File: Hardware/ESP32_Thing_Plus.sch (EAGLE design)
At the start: 40 parts, among them J1 AMP FCI 10103594-0001LF, Q1 2.5A/30V, Q2 MBT3904DW1T1, U1 MCP73831, U2 ESP-WROOM-32NARROW, U3 AP2112K-3.3V, U4 CP2102N

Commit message: v03 Changes
-Updated size to 2.3x0.9in
- Moved Qwiic connector to top
- Adjusted inner layer copper pour
- Cleaned up traces
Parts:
- added S2: 0, SparkFun-Switches:MOMENTARY-SWITCH-SPST-2-SMD-4.6X2.8MM
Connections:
- net 0: now also S2.4
- net GND: now also S2.1
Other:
- note added: "GPIO0 Button"
- note added: "Revised by: Alex Wende"
- note added: "v03"
- note removed: "02"
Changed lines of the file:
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@@
 <?xml version="1.0" encoding="utf-8"?>
 <!DOCTYPE eagle SYSTEM "eagle.dtd">
-<eagle version="9.0.1">
+<eagle version="9.1.1">
 <drawing>
 <settings>
@@
 <part name="FD3" library="SparkFun-Aesthetics" deviceset="FIDUCIAL" device="UFIDUCIAL"/>
 <part name="FD4" library="SparkFun-Aesthetics" deviceset="FIDUCIAL" device="UFIDUCIAL"/>
+<part name="S2" library="SparkFun-Switches" deviceset="MOMENTARY-SWITCH-SPST-2" device="-SMD-4.6X2.8MM" value="0"/>
+<part name="GND10" library="SparkFun-Aesthetics" deviceset="GND" device=""/>
 </parts>
 <sheets>
@@
 If U0TXD, GPIO2, GPIO5 are floating,
 GPIO0 determines boot mode</text>
-<text x="256.54" y="276.86" size="2.54" layer="94" font="vector" align="top-left">CP2102N (USB-to-Serial Converter)</text>
+<text x="256.54" y="274.32" size="2.54" layer="94" font="vector">CP2102N (USB-to-Serial Converter)</text>
 <text x="134.62" y="264.16" size="1.524" layer="97" align="top-left">V_BATT should be a single-
 cell LiPo battery.</text>
@@
 I_CHG = 1000 / R_PROG
 R_PROG=2k : I_CHG=500mA</text>
-<text x="2.54" y="276.86" size="2.54" layer="94" font="vector" align="top-left">Voltage Regulator and Battery Charger</text>
-<text x="132.08" y="276.86" size="2.54" layer="94" font="vector" align="top-left">Lithium-Polymer Battery Charger (1-cell)</text>
+<text x="2.54" y="274.32" size="2.54" layer="94" font="vector">Voltage Regulator and Battery Charger</text>
+<text x="132.08" y="274.32" size="2.54" layer="94" font="vector">Lithium-Polymer Battery Charger (1-cell)</text>
 <text x="86.36" y="220.98" size="1.778" layer="97" font="vector" align="top-center">600mA out
 6V max in</text>
-<text x="332.74" y="190.5" size="2.54" layer="94" font="vector" align="top-left">Auto-Reset</text>
+<text x="332.74" y="187.96" size="2.54" layer="94" font="vector">Auto-Reset</text>
 <wire x1="0" y1="193.04" x2="129.54" y2="193.04" width="0.2032" layer="97" style="longdash"/>
 <wire x1="129.54" y1="193.04" x2="254" y2="193.04" width="0.2032" layer="97" style="longdash"/>
@@
 <wire x1="259.08" y1="55.88" x2="259.08" y2="0" width="0.2032" layer="97" style="longdash"/>
 <wire x1="259.08" y1="55.88" x2="198.12" y2="55.88" width="0.2032" layer="97" style="longdash"/>
-<text x="2.54" y="190.5" size="2.54" layer="94" align="top-left">Espressif ESP32</text>
-<text x="261.62" y="63.5" size="2.54" layer="94" font="vector" align="top-left">Reset Button</text>
-<text x="332.74" y="104.14" size="2.54" layer="94" font="vector" align="top-left">Headers</text>
-<text x="421.64" y="10.16" size="2.54" layer="94" align="top-left">02</text>
+<text x="2.54" y="187.96" size="2.54" layer="94">Espressif ESP32</text>
+<text x="261.62" y="60.96" size="2.54" layer="94" font="vector">Reset Button</text>
+<text x="332.74" y="101.6" size="2.54" layer="94" font="vector">Headers</text>
+<text x="421.64" y="10.16" size="2.54" layer="94" align="top-left">v03</text>
 <text x="273.812" y="0.762" size="1.778" layer="94" rot="MR180" align="top-left">Original ESP32 Thing by Jim Lindblom</text>
 <text x="381" y="114.3" size="1.778" layer="97" font="vector" align="top-center">If DTR is LOW, toggling RTS from HIGH to LOW resets to run mode.
 If RTS is HIGH, toggling DTR from LOW to HIGH resets to bootloader.</text>
-<text x="264.16" y="187.96" size="2.54" layer="94" font="vector">QWIIC Connector</text>
+<text x="261.62" y="187.96" size="2.54" layer="94" font="vector">QWIIC Connector</text>
 <wire x1="259.08" y1="99.06" x2="259.08" y2="193.04" width="0.1524" layer="97" style="longdash"/>
-<text x="358.14" y="7.62" size="3.81" layer="94">Mike Hord</text>
+<text x="348.996" y="11.43" size="2.54" layer="94">Mike Hord</text>
 <text x="200.66" y="50.8" size="2.54" layer="94" font="vector">GPIO13 LED</text>
+<wire x1="259.08" y1="99.06" x2="259.08" y2="66.04" width="0.1524" layer="97" style="longdash"/>
+<text x="261.62" y="93.98" size="2.54" layer="94">GPIO0 Button</text>
+<text x="331.47" y="6.604" size="2.54" layer="94">Revised by: Alex Wende</text>
 </plain>
 <instances>
@@
 <instance part="FD3" gate="G$1" x="426.72" y="30.48"/>
 <instance part="FD4" gate="G$1" x="429.26" y="30.48"/>
+<instance part="S2" gate="G$1" x="294.64" y="83.82"/>
+<instance part="GND10" gate="1" x="287.02" y="78.74"/>
 </instances>
 <busses>
@@
 <pinref part="GND8" gate="1" pin="GND"/>
 <wire x1="185.42" y1="121.92" x2="185.42" y2="119.38" width="0.1524" layer="91"/>
+</segment>
+<segment>
+<pinref part="S2" gate="G$1" pin="1"/>
+<wire x1="289.56" y1="83.82" x2="287.02" y2="83.82" width="0.1524" layer="91"/>
+<wire x1="287.02" y1="83.82" x2="287.02" y2="81.28" width="0.1524" layer="91"/>
+<pinref part="GND10" gate="1" pin="GND"/>
 </segment>
 </net>
@@
 <label x="137.16" y="134.62" size="1.27" layer="95" xref="yes"/>
 </segment>
-</net>
+<segment>
+<label x="302.26" y="81.28" size="1.27" layer="95" font="vector" xref="yes"/>
+<pinref part="S2" gate="G$1" pin="4"/>
+<wire x1="299.72" y1="81.28" x2="302.26" y2="81.28" width="0.1524" layer="91"/>
+</segment>
+</net>

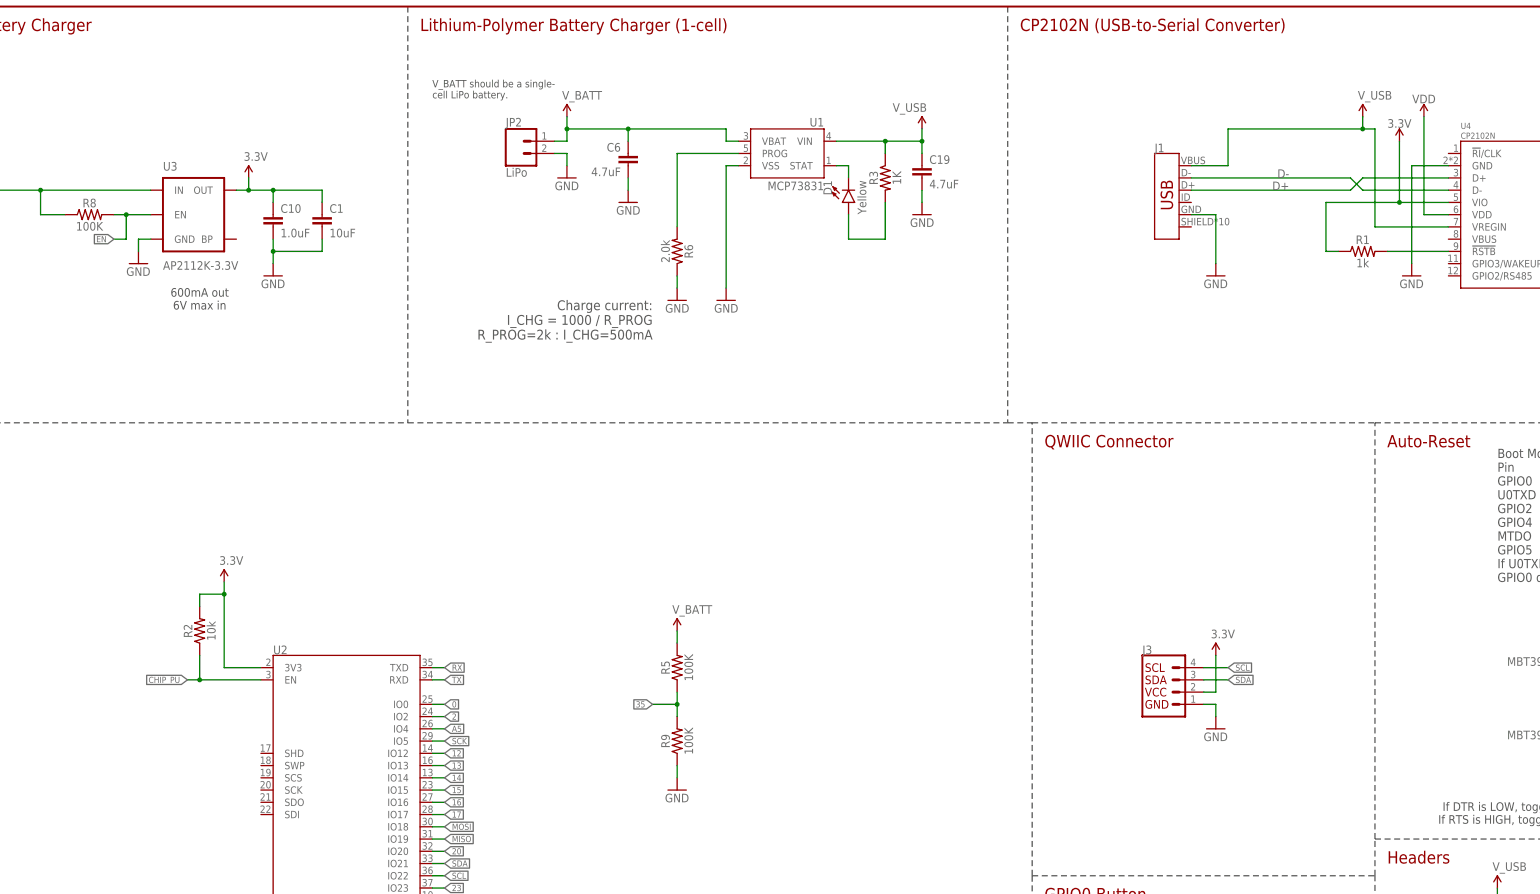
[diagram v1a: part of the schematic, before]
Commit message: V03 Changes Cont.
- Removed battery voltage divider
- Increased Board name silk on bottom
- Added NC buzzard labels to unconnected header pin.
- Added button to GPIO-0
- Swapped battery pins to match lipo battery pins
- Fixed missing pin connections on USB transceiver.
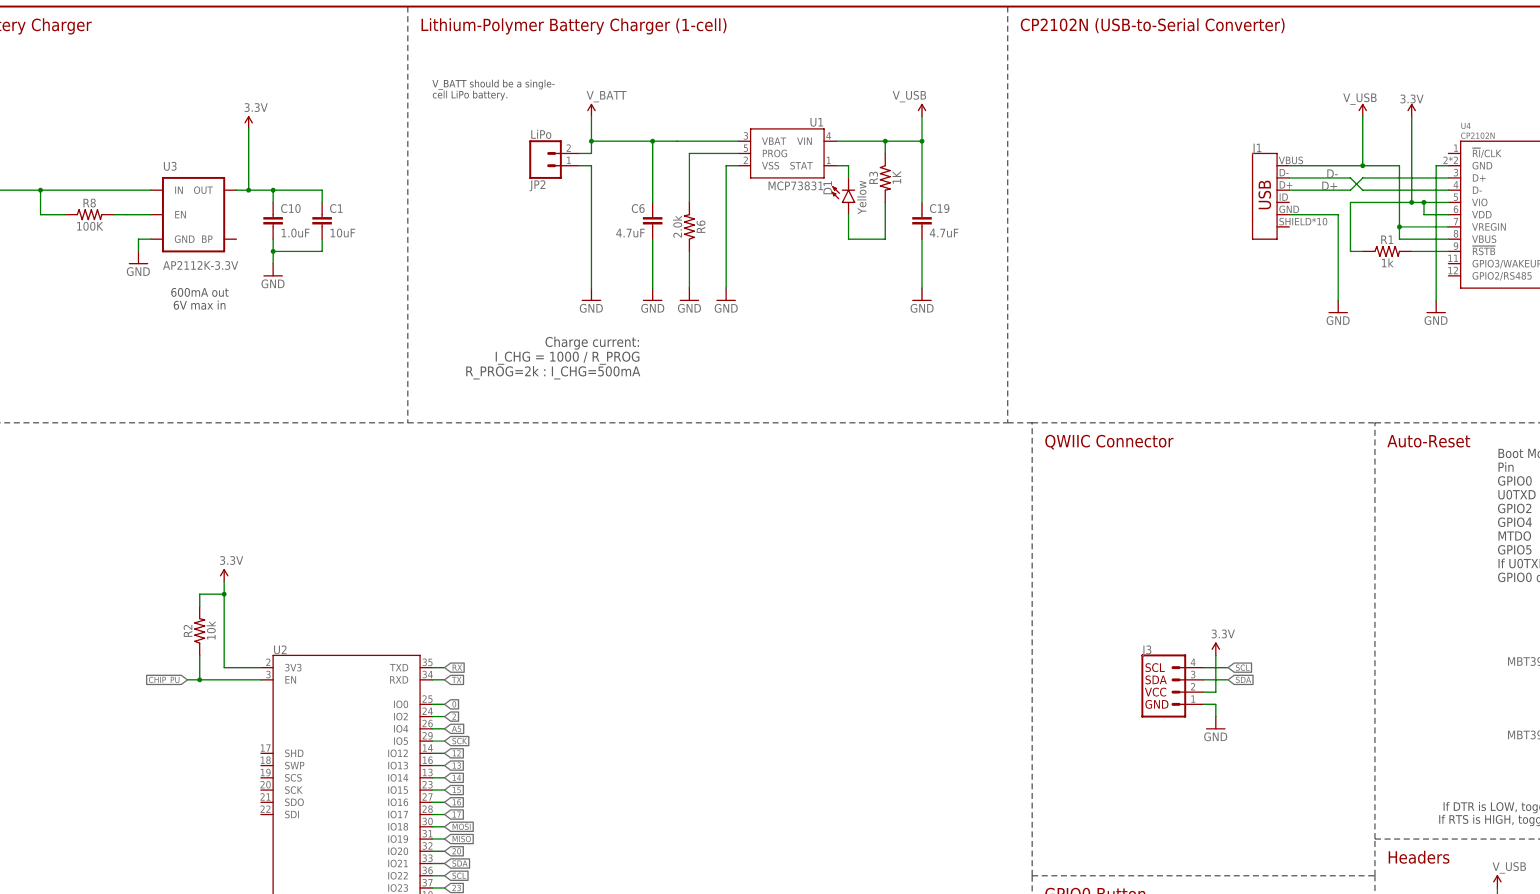
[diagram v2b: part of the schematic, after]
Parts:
- removed R5, R9: 100K, SparkFun-Resistors:100KOHM-0402-1/16W-1%
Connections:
- removed net VDD: U4.VDD
- net 3.3V: now also U4.VDD
- net 35: no longer R5.1, R9.2
- net GND: now also JP2.2; no longer JP2.1, R9.1
- net V_BATT: now also JP2.1; no longer JP2.2, R5.2
- net V_USB: now also U4.VBUS
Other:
- moved on the sheet: C19, C6, J1, JP2, R1, R6

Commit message: V03 QC Fixes
- Replaced via on GPIO0 with test point via
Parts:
- added TP1: TEST-POINTTP_15TH_THRU, SparkFun-Connectors:TEST-POINTTP_15TH_THRU
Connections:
- net 0: now also TP1.1
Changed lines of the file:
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@@
 <part name="S2" library="SparkFun-Switches" deviceset="MOMENTARY-SWITCH-SPST-2" device="-SMD-4.6X2.8MM" value="0"/>
 <part name="GND10" library="SparkFun-Aesthetics" deviceset="GND" device=""/>
+<part name="TP1" library="SparkFun-Connectors" deviceset="TEST-POINT" device="TP_15TH_THRU" value=""/>
 </parts>
 <sheets>
@@
 <instance part="S2" gate="G$1" x="294.64" y="83.82"/>
 <instance part="GND10" gate="1" x="287.02" y="78.74"/>
+<instance part="TP1" gate="G$1" x="309.88" y="81.28"/>
 </instances>
 <busses>
@@
 </segment>
 <segment>
-<label x="302.26" y="81.28" size="1.27" layer="95" font="vector" xref="yes"/>
 <pinref part="S2" gate="G$1" pin="4"/>
-<wire x1="299.72" y1="81.28" x2="302.26" y2="81.28" width="0.1524" layer="91"/>
-</segment>
-</net>
+<pinref part="TP1" gate="G$1" pin="1"/>
+<wire x1="299.72" y1="81.28" x2="309.88" y2="81.28" width="0.1524" layer="91"/>
+<label x="304.546" y="81.534" size="1.778" layer="95"/>
+</segment>
+</net>

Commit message: v10
-Updated silk to include pin numbers and seondary functions for SPI/I2C/UART
-Remapped a couple outer pins to match board definitions file
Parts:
- removed J1: AMP FCI 10103594-0001LF, SparkFun-Connectors:USB_MICRO-B_HALF_PTH_MILL
- added J5: (no value), SparkFun-Connectors:USB_MICRO-B_HALF_PTH
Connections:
- removed net 23: J4.16, U2.IO23
- new net 21: J4.16, U2.IO21
- net 12: now also J2.5
- net 20: no longer J2.5
- net D+: now also J5.D+; no longer J1.D+
- net D-: now also J5.D-; no longer J1.D-
- net GND: now also J5.GND; no longer J1.GND
- net SDA: now also U2.IO23; no longer U2.IO21
- net V_USB: now also J5.VBUS; no longer J1.VBUS
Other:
- note added: "v10"
- note removed: "v03"
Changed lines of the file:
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@@
 <part name="SUPPLY1" library="SparkFun-Aesthetics" deviceset="3.3V" device=""/>
 <part name="GND6" library="SparkFun-Aesthetics" deviceset="GND" device=""/>
-<part name="J1" library="SparkFun-Connectors" deviceset="USB_MICRO-B" device="_HALF_PTH_MILL" value="AMP FCI 10103594-0001LF"/>
 <part name="U4" library="SparkFun-IC-Comms" deviceset="CP2102N" device=""/>
 <part name="R1" library="SparkFun-Resistors" deviceset="1KOHM" device="-0603-1/10W-1%" value="1k"/>
@@
 <part name="GND10" library="SparkFun-Aesthetics" deviceset="GND" device=""/>
 <part name="TP1" library="SparkFun-Connectors" deviceset="TEST-POINT" device="TP_15TH_THRU" value=""/>
+<part name="J5" library="SparkFun-Connectors" deviceset="USB_MICRO-B" device="_HALF_PTH"/>
 </parts>
 <sheets>
@@
 <text x="261.62" y="60.96" size="2.54" layer="94" font="vector">Reset Button</text>
 <text x="332.74" y="101.6" size="2.54" layer="94" font="vector">Headers</text>
-<text x="421.64" y="10.16" size="2.54" layer="94" align="top-left">v03</text>
+<text x="421.64" y="10.16" size="2.54" layer="94" align="top-left">v10</text>
 <text x="273.812" y="0.762" size="1.778" layer="94" rot="MR180" align="top-left">Original ESP32 Thing by Jim Lindblom</text>
 <text x="381" y="114.3" size="1.778" layer="97" font="vector" align="top-center">If DTR is LOW, toggling RTS from HIGH to LOW resets to run mode.
@@
 <instance part="SUPPLY1" gate="G$1" x="297.18" y="144.78"/>
 <instance part="GND6" gate="1" x="297.18" y="129.54"/>
-<instance part="J1" gate="J1" x="307.34" y="238.76" smashed="yes">
-<attribute name="NAME" x="304.8" y="249.174" size="1.778" layer="95" font="vector"/>
-</instance>
 <instance part="U4" gate="G$1" x="365.76" y="236.22"/>
 <instance part="R1" gate="G$1" x="332.74" y="228.6"/>
@@
 <instance part="GND10" gate="1" x="287.02" y="78.74"/>
 <instance part="TP1" gate="G$1" x="309.88" y="81.28"/>
+<instance part="J5" gate="J1" x="294.64" y="238.76"/>
 </instances>
 <busses>
@@
 <wire x1="322.58" y1="236.22" x2="322.58" y2="218.44" width="0.1524" layer="91"/>
 <wire x1="322.58" y1="236.22" x2="312.42" y2="236.22" width="0.1524" layer="91"/>
-<pinref part="J1" gate="J1" pin="GND"/>
+<pinref part="J5" gate="J1" pin="GND"/>
+<wire x1="312.42" y1="236.22" x2="299.72" y2="236.22" width="0.1524" layer="91"/>
 </segment>
 <segment>
@@
 <wire x1="335.28" y1="233.68" x2="345.44" y2="233.68" width="0.1524" layer="91"/>
 <wire x1="314.96" y1="246.38" x2="312.42" y2="246.38" width="0.1524" layer="91"/>
-<pinref part="J1" gate="J1" pin="VBUS"/>
 <wire x1="314.96" y1="246.38" x2="327.66" y2="246.38" width="0.1524" layer="91"/>
 <pinref part="U4" gate="G$1" pin="VBUS"/>
@@
 <wire x1="335.28" y1="231.14" x2="335.28" y2="233.68" width="0.1524" layer="91"/>
 <junction x="335.28" y="233.68"/>
+<pinref part="J5" gate="J1" pin="VBUS"/>
+<wire x1="312.42" y1="246.38" x2="299.72" y2="246.38" width="0.1524" layer="91"/>
 </segment>
 <segment>
@@
 <label x="322.58" y="243.84" size="1.778" layer="95" rot="MR0"/>
 <wire x1="325.12" y1="243.84" x2="312.42" y2="243.84" width="0.1524" layer="91"/>
-<pinref part="J1" gate="J1" pin="D-"/>
 <wire x1="325.12" y1="243.84" x2="327.66" y2="241.3" width="0.1524" layer="91"/>
 <pinref part="U4" gate="G$1" pin="D-"/>
 <wire x1="327.66" y1="241.3" x2="345.44" y2="241.3" width="0.1524" layer="91"/>
+<pinref part="J5" gate="J1" pin="D-"/>
+<wire x1="312.42" y1="243.84" x2="299.72" y2="243.84" width="0.1524" layer="91"/>
 </segment>
 </net>
@@
 <label x="322.58" y="241.3" size="1.778" layer="95" rot="MR0"/>
 <wire x1="325.12" y1="241.3" x2="312.42" y2="241.3" width="0.1524" layer="91"/>
-<pinref part="J1" gate="J1" pin="D+"/>
 <wire x1="325.12" y1="241.3" x2="327.66" y2="243.84" width="0.1524" layer="91"/>
 <pinref part="U4" gate="G$1" pin="D+"/>
 <wire x1="327.66" y1="243.84" x2="345.44" y2="243.84" width="0.1524" layer="91"/>
+<pinref part="J5" gate="J1" pin="D+"/>
+<wire x1="312.42" y1="241.3" x2="299.72" y2="241.3" width="0.1524" layer="91"/>
 </segment>
 </net>
@@
 </segment>
 <segment>
-<pinref part="U2" gate="G$1" pin="IO21"/>
-<wire x1="134.62" y1="101.6" x2="137.16" y2="101.6" width="0.1524" layer="91"/>
-<label x="137.16" y="101.6" size="1.27" layer="95" xref="yes"/>
-</segment>
-<segment>
 <pinref part="J3" gate="G$1" pin="3"/>
 <wire x1="294.64" y1="139.7" x2="299.72" y2="139.7" width="0.1524" layer="91"/>
 <label x="299.72" y="139.7" size="1.27" layer="95" xref="yes"/>
 </segment>
+<segment>
+<pinref part="U2" gate="G$1" pin="IO23"/>
+<wire x1="134.62" y1="96.52" x2="137.16" y2="96.52" width="0.1524" layer="91"/>
+<label x="137.16" y="96.52" size="1.27" layer="95" xref="yes"/>
+</segment>
 </net>
 <net name="SCL" class="0">
@@
 <wire x1="134.62" y1="124.46" x2="137.16" y2="124.46" width="0.1524" layer="91"/>
 <label x="137.16" y="124.46" size="1.27" layer="95" xref="yes"/>
+</segment>
+<segment>
+<pinref part="J2" gate="G$1" pin="5"/>
+<wire x1="368.3" y1="81.28" x2="365.76" y2="81.28" width="0.1524" layer="91"/>
+<label x="365.76" y="81.28" size="1.27" layer="95" rot="R180" xref="yes"/>
 </segment>
 </net>
@@
 </segment>
 </net>
-<net name="23" class="0">
-<segment>
-<pinref part="U2" gate="G$1" pin="IO23"/>
-<wire x1="134.62" y1="96.52" x2="137.16" y2="96.52" width="0.1524" layer="91"/>
-<label x="137.16" y="96.52" size="1.27" layer="95" xref="yes"/>
-</segment>
-<segment>
-<pinref part="J4" gate="G$1" pin="16"/>
-<wire x1="393.7" y1="53.34" x2="396.24" y2="53.34" width="0.1524" layer="91"/>
-<label x="396.24" y="53.34" size="1.27" layer="95" xref="yes"/>
-</segment>
-</net>
 <net name="35" class="0">
 <segment>
@@
 <wire x1="134.62" y1="104.14" x2="137.16" y2="104.14" width="0.1524" layer="91"/>
 <label x="137.16" y="104.14" size="1.27" layer="95" xref="yes"/>
-</segment>
-<segment>
-<pinref part="J2" gate="G$1" pin="5"/>
-<wire x1="368.3" y1="81.28" x2="365.76" y2="81.28" width="0.1524" layer="91"/>
-<label x="365.76" y="81.28" size="1.27" layer="95" rot="R180" xref="yes"/>
 </segment>
 </net>
@@
 </segment>
 </net>
+<net name="21" class="0">
+<segment>
+<pinref part="U2" gate="G$1" pin="IO21"/>
+<wire x1="134.62" y1="101.6" x2="137.16" y2="101.6" width="0.1524" layer="91"/>
+<label x="137.16" y="101.6" size="1.27" layer="95" xref="yes"/>
+</segment>
+<segment>
+<pinref part="J4" gate="G$1" pin="16"/>
+<wire x1="393.7" y1="53.34" x2="396.24" y2="53.34" width="0.1524" layer="91"/>
+<label x="396.24" y="53.34" size="1.27" layer="95" xref="yes"/>
+</segment>
+</net>

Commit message: v10 design review changes
- Moved battery connector away from headers by 0.030"
- Moved charge led and resistor away from standoff
- Fixed silk on header pins 21 and 12
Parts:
- D2: value BAT20J -> 1A/23V/620mV
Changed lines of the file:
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@@
 <part name="GND12" library="SparkFun-Aesthetics" deviceset="GND" device=""/>
 <part name="C6" library="SparkFun-Capacitors" deviceset="4.7UF" device="0603" value="4.7uF"/>
-<part name="D2" library="SparkFun-DiscreteSemi" deviceset="DIODE-SCHOTTKY" device="-BAT20J" value="BAT20J"/>
+<part name="D2" library="SparkFun-DiscreteSemi" deviceset="DIODE-SCHOTTKY" device="-BAT20J" value="1A/23V/620mV"/>
 <part name="R7" library="SparkFun-Resistors" deviceset="10KOHM" device="-0603-1/10W-1%" value="10k"/>
 <part name="GND13" library="SparkFun-Aesthetics" deviceset="GND" device=""/>

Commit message: v10 design review changes cont.
Fixed pin 1 marker on dual NPN transistor
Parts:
- Q2: device esp32-thing-temp:MBT3904DW1T1 -> SparkFun-DiscreteSemi:TRANS_NPN_DUAL-MBT3904DW1T1
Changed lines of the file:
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@@
 <part name="R18" library="SparkFun-Resistors" deviceset="10KOHM" device="-0603-1/10W-1%" value="10k"/>
 <part name="SUPPLY8" library="SparkFun-Aesthetics" deviceset="3.3V" device=""/>
-<part name="Q2" library="esp32-thing-temp" deviceset="MBT3904DW1T1" device="" value="MBT3904DW1T1"/>
+<part name="Q2" library="SparkFun-DiscreteSemi" deviceset="TRANS_NPN_DUAL" device="-MBT3904DW1T1" value="MBT3904DW1T1"/>
 <part name="LOGO2" library="SparkFun-Aesthetics" deviceset="OSHW-LOGO" device="MINI" value="OSHW-LOGOMINI"/>
 <part name="J3" library="SparkFun-Connectors" deviceset="QWIIC_CONNECTOR" device="JS-1MM"/>

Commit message: v10 QC Fixes
- Replaced drill hit with standoff
- Added VCC range and battery type to schematic
- Updated USB connector
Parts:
- added H1, H2: STAND-OFFTIGHT, SparkFun-Hardware:STAND-OFFTIGHT
- J5: device SparkFun-Connectors:USB_MICRO-B_HALF_PTH -> SparkFun-Connectors:USB_MICRO-B_HALF_PTH_MILL
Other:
- note added: "V_USB - 6V MAX V_BATT - Single Cell (4.2V MAX)"
- moved on the sheet: J5
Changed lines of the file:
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@@
 <part name="GND10" library="SparkFun-Aesthetics" deviceset="GND" device=""/>
 <part name="TP1" library="SparkFun-Connectors" deviceset="TEST-POINT" device="TP_15TH_THRU" value=""/>
-<part name="J5" library="SparkFun-Connectors" deviceset="USB_MICRO-B" device="_HALF_PTH"/>
+<part name="J5" library="SparkFun-Connectors" deviceset="USB_MICRO-B" device="_HALF_PTH_MILL"/>
+<part name="H1" library="SparkFun-Hardware" deviceset="STAND-OFF" device="TIGHT"/>
+<part name="H2" library="SparkFun-Hardware" deviceset="STAND-OFF" device="TIGHT"/>
 </parts>
 <sheets>
@@
 <text x="261.62" y="93.98" size="2.54" layer="94">GPIO0 Button</text>
 <text x="331.47" y="6.604" size="2.54" layer="94">Revised by: Alex Wende</text>
+<text x="12.7" y="266.7" size="1.778" layer="97">V_USB - 6V MAX
+V_BATT - Single Cell (4.2V MAX)</text>
 </plain>
 <instances>
@@
 <instance part="TP1" gate="G$1" x="309.88" y="81.28"/>
 <instance part="J5" gate="J1" x="294.64" y="238.76"/>
+<instance part="H1" gate="G$1" x="421.64" y="33.02"/>
+<instance part="H2" gate="G$1" x="421.64" y="30.48"/>
 </instances>
 <busses>
